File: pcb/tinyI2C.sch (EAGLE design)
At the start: 37 parts, among them IC1 74LVC1G125DCK, IC2 74LVC1G125DCK, IC3 IC_LDO_MIC5355, U1 LPC824M201JHI33, X1 TSW-112-02-S-S, X2 TSW-112-02-S-S, X3 TSW-106-02-S-S-RA, X4 TSW-102-02-S-S, X5 TSW-102-02-S-S, X6 TSW-102-02-S-S

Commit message: [ PCB ][ SCH ] R, C, BOM
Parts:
- C1, C2, C6, C7: value 1005 -> 0.1u/1005
- C3, C4, C5: value 1005 -> 10u/1005
- C8, C9: value 1005 -> 18p/1005
- Q1: value (none) -> 12MHz
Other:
- moved on the sheet: C2, C3, C4, C5, C6, IC3, TP1, TP2, TP3, TP6, TP7, X4-2

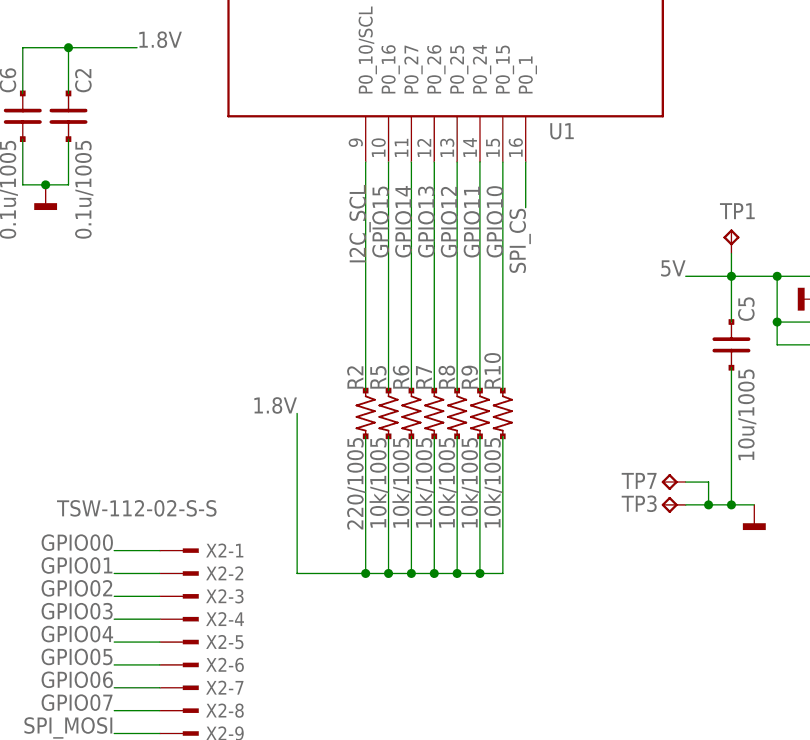
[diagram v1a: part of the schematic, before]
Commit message: [ PCB ] Q1 silk
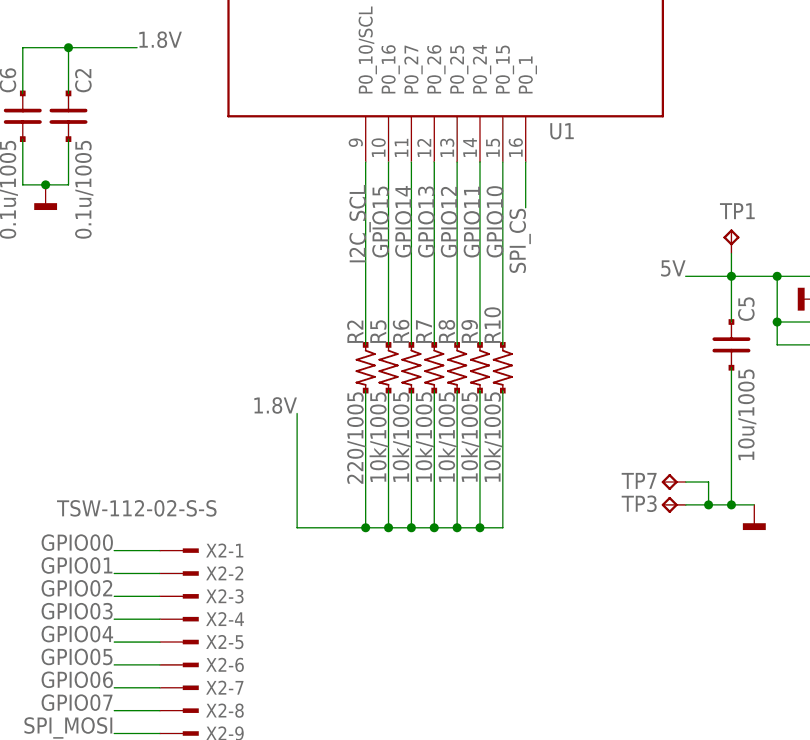
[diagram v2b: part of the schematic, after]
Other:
- moved on the sheet: R10, R2, R5, R6, R7, R8, R9
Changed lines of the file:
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@@
 </instance>
 <instance part="R1" gate="G$1" x="81.28" y="129.54" rot="R90"/>
-<instance part="R2" gate="G$1" x="127" y="55.88" rot="R270"/>
+<instance part="R2" gate="G$1" x="127" y="60.96" rot="R270"/>
 <instance part="R3" gate="G$1" x="86.36" y="129.54" rot="R90"/>
 <instance part="R4" gate="G$1" x="83.82" y="129.54" rot="R90"/>
-<instance part="R5" gate="G$1" x="129.54" y="55.88" rot="R270"/>
-<instance part="R6" gate="G$1" x="132.08" y="55.88" rot="R270"/>
-<instance part="R7" gate="G$1" x="134.62" y="55.88" rot="R270"/>
-<instance part="R8" gate="G$1" x="137.16" y="55.88" rot="R270"/>
-<instance part="R9" gate="G$1" x="139.7" y="55.88" rot="R270"/>
-<instance part="R10" gate="G$1" x="142.24" y="55.88" rot="R270"/>
+<instance part="R5" gate="G$1" x="129.54" y="60.96" rot="R270"/>
+<instance part="R6" gate="G$1" x="132.08" y="60.96" rot="R270"/>
+<instance part="R7" gate="G$1" x="134.62" y="60.96" rot="R270"/>
+<instance part="R8" gate="G$1" x="137.16" y="60.96" rot="R270"/>
+<instance part="R9" gate="G$1" x="139.7" y="60.96" rot="R270"/>
+<instance part="R10" gate="G$1" x="142.24" y="60.96" rot="R270"/>
 <instance part="C3" gate="G$1" x="231.14" y="63.5"/>
 <instance part="GND1" gate="1" x="231.14" y="48.26"/>
@@
 <segment>
 <pinref part="R2" gate="G$1" pin="2"/>
-<wire x1="127" y1="53.34" x2="127" y2="38.1" width="0.1524" layer="91"/>
+<wire x1="127" y1="58.42" x2="127" y2="43.18" width="0.1524" layer="91"/>
 <label x="119.38" y="55.88" size="1.778" layer="95" rot="MR0"/>
 <pinref part="R5" gate="G$1" pin="2"/>
-<wire x1="127" y1="38.1" x2="119.38" y2="38.1" width="0.1524" layer="91"/>
-<wire x1="119.38" y1="38.1" x2="119.38" y2="55.88" width="0.1524" layer="91"/>
-<wire x1="129.54" y1="53.34" x2="129.54" y2="38.1" width="0.1524" layer="91"/>
-<wire x1="129.54" y1="38.1" x2="127" y2="38.1" width="0.1524" layer="91"/>
-<junction x="127" y="38.1"/>
+<wire x1="127" y1="43.18" x2="119.38" y2="43.18" width="0.1524" layer="91"/>
+<wire x1="119.38" y1="43.18" x2="119.38" y2="55.88" width="0.1524" layer="91"/>
+<wire x1="129.54" y1="58.42" x2="129.54" y2="43.18" width="0.1524" layer="91"/>
+<wire x1="129.54" y1="43.18" x2="127" y2="43.18" width="0.1524" layer="91"/>
+<junction x="127" y="43.18"/>
 <pinref part="R6" gate="G$1" pin="2"/>
-<wire x1="132.08" y1="53.34" x2="132.08" y2="38.1" width="0.1524" layer="91"/>
-<wire x1="132.08" y1="38.1" x2="129.54" y2="38.1" width="0.1524" layer="91"/>
-<junction x="129.54" y="38.1"/>
+<wire x1="132.08" y1="58.42" x2="132.08" y2="43.18" width="0.1524" layer="91"/>
+<wire x1="132.08" y1="43.18" x2="129.54" y2="43.18" width="0.1524" layer="91"/>
+<junction x="129.54" y="43.18"/>
 <pinref part="R7" gate="G$1" pin="2"/>
-<wire x1="134.62" y1="53.34" x2="134.62" y2="38.1" width="0.1524" layer="91"/>
-<wire x1="134.62" y1="38.1" x2="132.08" y2="38.1" width="0.1524" layer="91"/>
-<junction x="132.08" y="38.1"/>
+<wire x1="134.62" y1="58.42" x2="134.62" y2="43.18" width="0.1524" layer="91"/>
+<wire x1="134.62" y1="43.18" x2="132.08" y2="43.18" width="0.1524" layer="91"/>
+<junction x="132.08" y="43.18"/>
 <pinref part="R8" gate="G$1" pin="2"/>
-<wire x1="137.16" y1="53.34" x2="137.16" y2="38.1" width="0.1524" layer="91"/>
-<wire x1="137.16" y1="38.1" x2="134.62" y2="38.1" width="0.1524" layer="91"/>
-<junction x="134.62" y="38.1"/>
+<wire x1="137.16" y1="58.42" x2="137.16" y2="43.18" width="0.1524" layer="91"/>
+<wire x1="137.16" y1="43.18" x2="134.62" y2="43.18" width="0.1524" layer="91"/>
+<junction x="134.62" y="43.18"/>
 <pinref part="R9" gate="G$1" pin="2"/>
-<wire x1="139.7" y1="53.34" x2="139.7" y2="38.1" width="0.1524" layer="91"/>
-<wire x1="139.7" y1="38.1" x2="137.16" y2="38.1" width="0.1524" layer="91"/>
-<junction x="137.16" y="38.1"/>
+<wire x1="139.7" y1="58.42" x2="139.7" y2="43.18" width="0.1524" layer="91"/>
+<wire x1="139.7" y1="43.18" x2="137.16" y2="43.18" width="0.1524" layer="91"/>
+<junction x="137.16" y="43.18"/>
 <pinref part="R10" gate="G$1" pin="2"/>
-<wire x1="142.24" y1="53.34" x2="142.24" y2="38.1" width="0.1524" layer="91"/>
-<wire x1="142.24" y1="38.1" x2="139.7" y2="38.1" width="0.1524" layer="91"/>
-<junction x="139.7" y="38.1"/>
+<wire x1="142.24" y1="58.42" x2="142.24" y2="43.18" width="0.1524" layer="91"/>
+<wire x1="142.24" y1="43.18" x2="139.7" y2="43.18" width="0.1524" layer="91"/>
+<junction x="139.7" y="43.18"/>
 </segment>
 <segment>
@@
 <pinref part="U1" gate="G$1" pin="P0_10/SCL"/>
 <label x="127" y="81.28" size="1.778" layer="95" rot="MR270"/>
-<wire x1="127" y1="83.82" x2="127" y2="58.42" width="0.1524" layer="91"/>
+<wire x1="127" y1="83.82" x2="127" y2="63.5" width="0.1524" layer="91"/>
 <pinref part="R2" gate="G$1" pin="1"/>
 </segment>
@@
 <pinref part="U1" gate="G$1" pin="P0_16"/>
 <label x="129.54" y="81.28" size="1.778" layer="95" rot="MR270"/>
-<wire x1="129.54" y1="83.82" x2="129.54" y2="58.42" width="0.1524" layer="91"/>
+<wire x1="129.54" y1="83.82" x2="129.54" y2="63.5" width="0.1524" layer="91"/>
 <pinref part="R5" gate="G$1" pin="1"/>
 </segment>
@@
 <label x="132.08" y="81.28" size="1.778" layer="95" rot="MR270"/>
 <pinref part="R6" gate="G$1" pin="1"/>
-<wire x1="132.08" y1="58.42" x2="132.08" y2="83.82" width="0.1524" layer="91"/>
+<wire x1="132.08" y1="63.5" x2="132.08" y2="83.82" width="0.1524" layer="91"/>
 </segment>
 <segment>
@@
 <label x="134.62" y="81.28" size="1.778" layer="95" rot="MR270"/>
 <pinref part="R7" gate="G$1" pin="1"/>
-<wire x1="134.62" y1="58.42" x2="134.62" y2="83.82" width="0.1524" layer="91"/>
+<wire x1="134.62" y1="63.5" x2="134.62" y2="83.82" width="0.1524" layer="91"/>
 </segment>
 <segment>
@@
 <label x="137.16" y="81.28" size="1.778" layer="95" rot="MR270"/>
 <pinref part="R8" gate="G$1" pin="1"/>
-<wire x1="137.16" y1="58.42" x2="137.16" y2="83.82" width="0.1524" layer="91"/>
+<wire x1="137.16" y1="63.5" x2="137.16" y2="83.82" width="0.1524" layer="91"/>
 </segment>
 <segment>
@@
 <label x="139.7" y="81.28" size="1.778" layer="95" rot="MR270"/>
 <pinref part="R9" gate="G$1" pin="1"/>
-<wire x1="139.7" y1="58.42" x2="139.7" y2="83.82" width="0.1524" layer="91"/>
+<wire x1="139.7" y1="63.5" x2="139.7" y2="83.82" width="0.1524" layer="91"/>
 </segment>
 <segment>
@@
 <label x="142.24" y="81.28" size="1.778" layer="95" rot="MR270"/>
 <pinref part="R10" gate="G$1" pin="1"/>
-<wire x1="142.24" y1="58.42" x2="142.24" y2="83.82" width="0.1524" layer="91"/>
-</segment>
-<segment>
+<wire x1="142.24" y1="63.5" x2="142.24" y2="83.82" width="0.1524" layer="91"/>
+</segment>
+<segment>

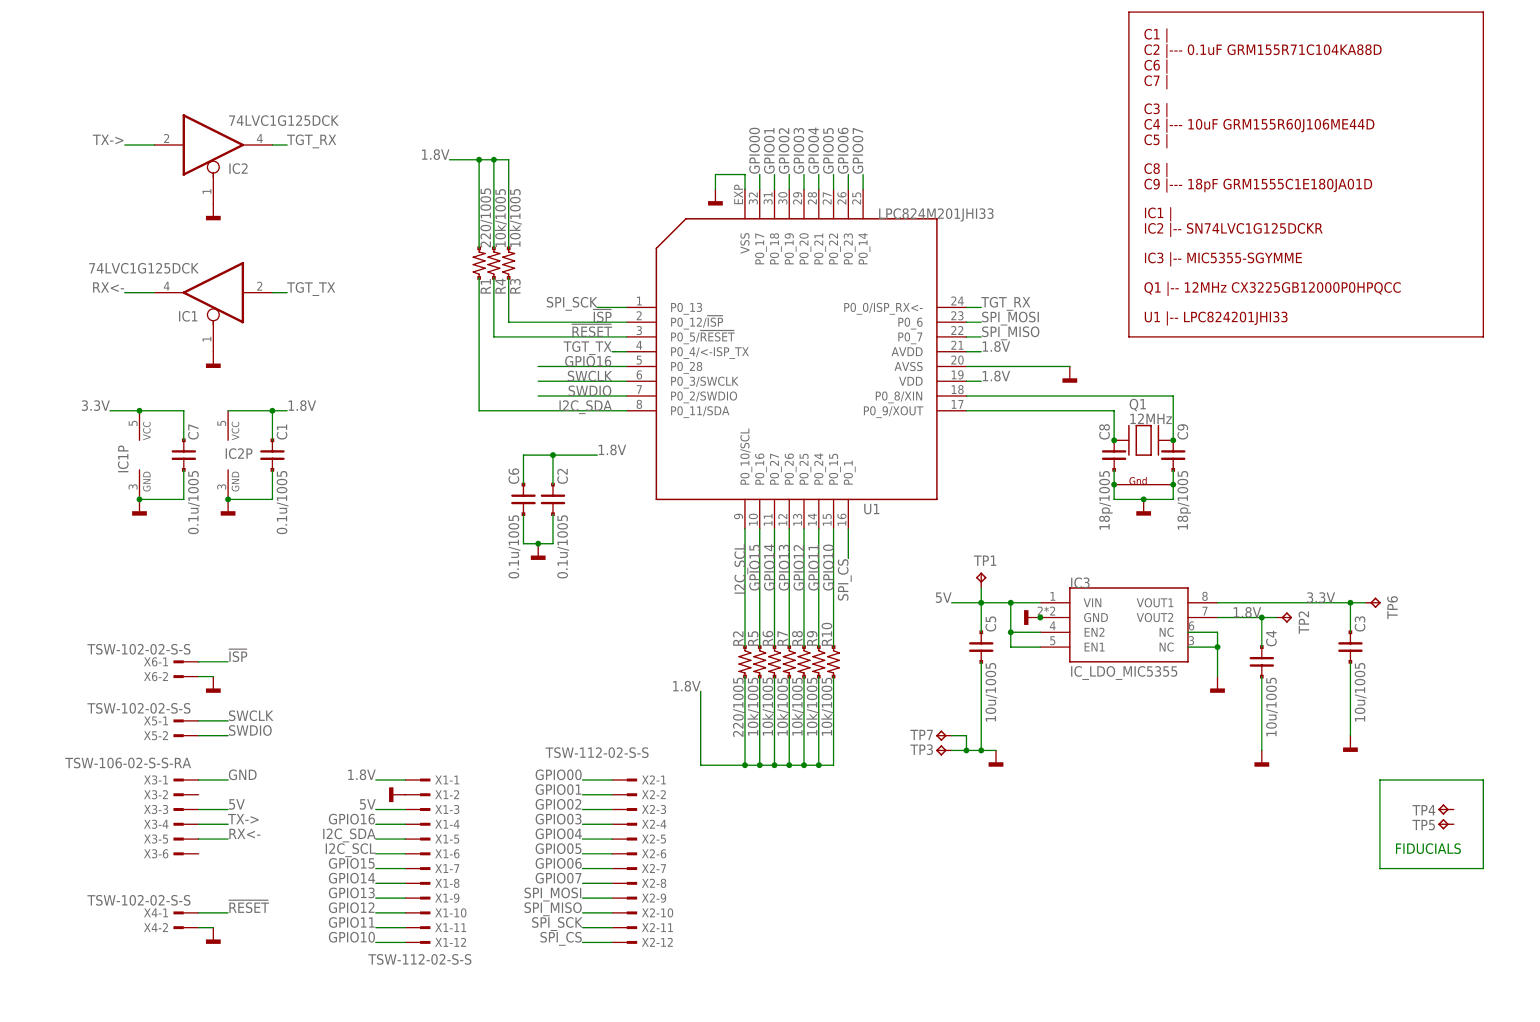
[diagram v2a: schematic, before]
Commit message: [ PCB ] add minlab icon;panel fix
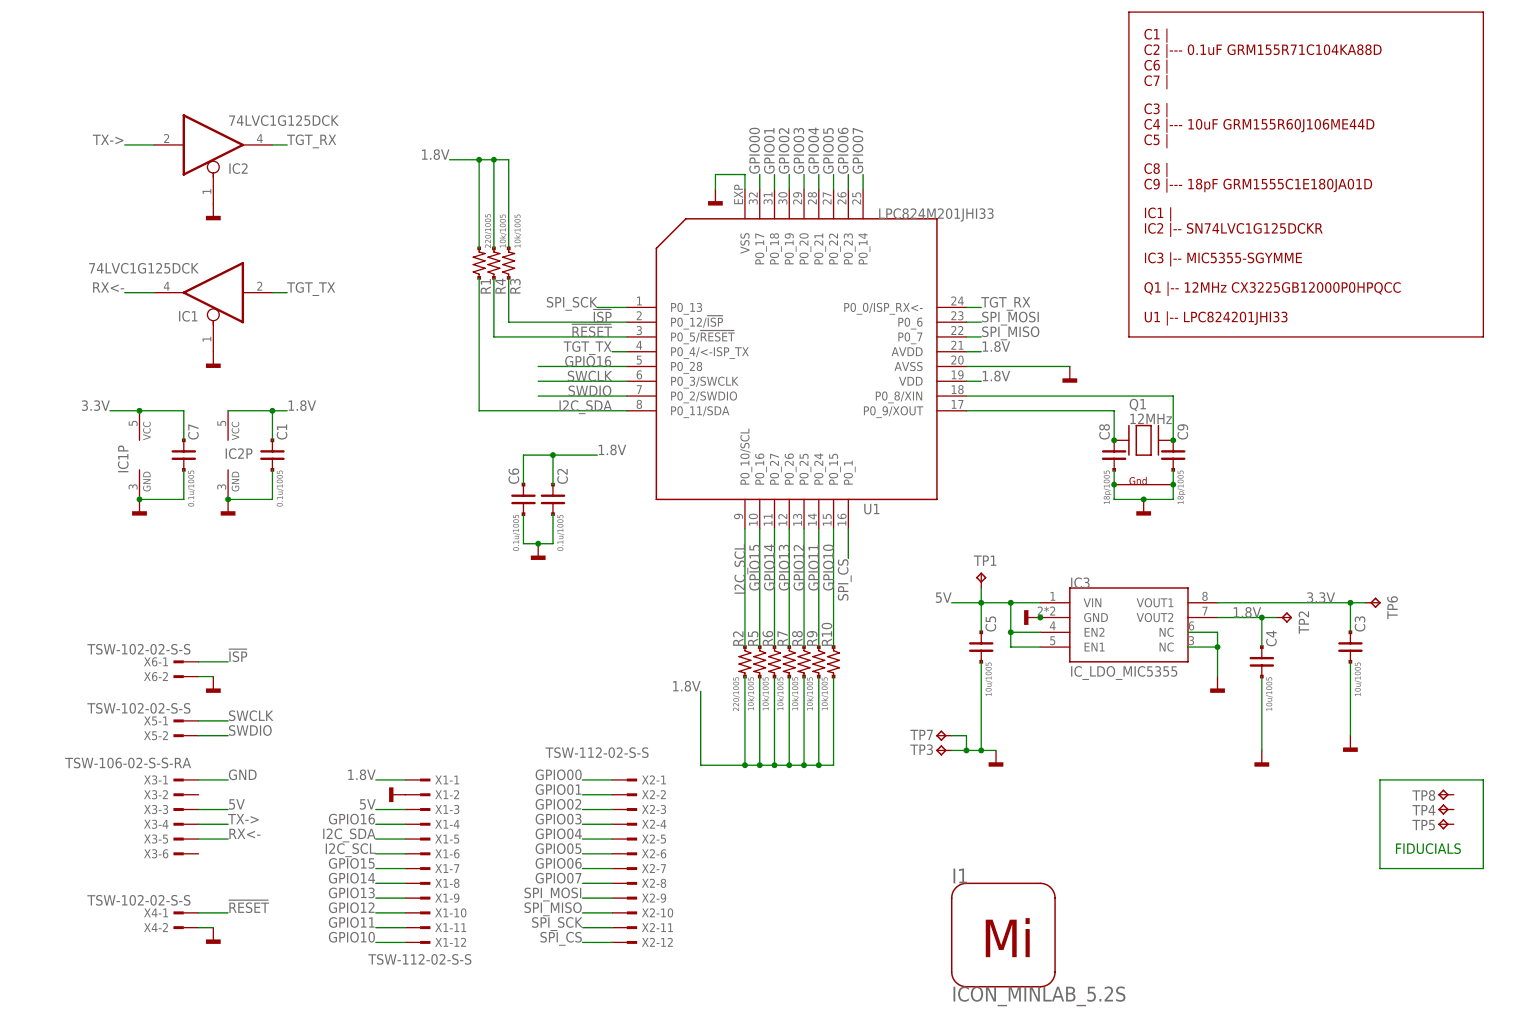
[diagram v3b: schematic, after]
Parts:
- added I1: ICON_MINLAB_5.2S, mylib:ICON_MINLAB_5.2S
- added TP8: TPTP10R, testpad:TPTP10R
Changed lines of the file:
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@@
 <layer number="132" name="bAdjust" color="7" fill="1" visible="no" active="yes"/>
 <layer number="144" name="Drill_legend" color="7" fill="1" visible="no" active="yes"/>
+<layer number="145" name="DrillLegend_01-16" color="2" fill="9" visible="no" active="yes"/>
+<layer number="146" name="DrillLegend_01-20" color="3" fill="9" visible="no" active="yes"/>
 <layer number="151" name="HeatSink" color="7" fill="1" visible="no" active="yes"/>
 <layer number="152" name="_bDocu" color="7" fill="1" visible="no" active="yes"/>
@@
 <part name="GND16" library="mbed-HDK" deviceset="GND" device=""/>
 <part name="TP7" library="testpad_local" deviceset="TP" device="B1,27" value="TPB1,27"/>
+<part name="TP8" library="testpad" deviceset="TP" device="TP10R" value="TPTP10R"/>
+<part name="I1" library="mylib" deviceset="ICON_MINLAB" device="_5.2S" value="ICON_MINLAB_5.2S"/>
 </parts>
 <sheets>
@@
 <attribute name="TP_SIGNAL_NAME" x="161.29" y="49.53" size="1.778" layer="97" rot="R90"/>
 </instance>
+<instance part="TP8" gate="G$1" x="246.38" y="38.1" smashed="yes" rot="R90">
+<attribute name="NAME" x="245.872" y="37.084" size="1.778" layer="95" rot="MR0"/>
+<attribute name="TP_SIGNAL_NAME" x="247.65" y="39.37" size="1.778" layer="97" rot="R90"/>
+</instance>
+<instance part="I1" gate="G$1" x="162.56" y="5.08"/>
 </instances>
 <busses>

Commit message: [ PCB ] library update
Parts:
- TP4, TP5, TP8: value TPTP10R -> TPTP20R; device testpad:TPTP10R -> testpad_local:TPTP20R
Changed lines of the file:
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@@
 <layers>
 <layer number="1" name="Top" color="4" fill="1" visible="no" active="no"/>
+<layer number="2" name="Route2" color="1" fill="3" visible="no" active="no"/>
+<layer number="3" name="Route3" color="4" fill="3" visible="no" active="no"/>
+<layer number="14" name="Route14" color="1" fill="6" visible="no" active="no"/>
+<layer number="15" name="Route15" color="4" fill="6" visible="no" active="no"/>
 <layer number="16" name="Bottom" color="1" fill="1" visible="no" active="no"/>
 <layer number="17" name="Pads" color="2" fill="1" visible="no" active="no"/>
@@
 <part name="X4" library="con-samtec.local" deviceset="TSW-102-02-S-S" device=""/>
 <part name="GND12" library="mbed-HDK" deviceset="GND" device=""/>
-<part name="TP4" library="testpad" deviceset="TP" device="TP10R" value="TPTP10R"/>
-<part name="TP5" library="testpad" deviceset="TP" device="TP10R" value="TPTP10R"/>
+<part name="TP4" library="testpad_local" deviceset="TP" device="TP20R" value="TPTP20R"/>
+<part name="TP5" library="testpad_local" deviceset="TP" device="TP20R" value="TPTP20R"/>
 <part name="X5" library="con-samtec.local" deviceset="TSW-102-02-S-S" device=""/>
 <part name="X6" library="con-samtec.local" deviceset="TSW-102-02-S-S" device=""/>
@@
 <part name="GND16" library="mbed-HDK" deviceset="GND" device=""/>
 <part name="TP7" library="testpad_local" deviceset="TP" device="B1,27" value="TPB1,27"/>
-<part name="TP8" library="testpad" deviceset="TP" device="TP10R" value="TPTP10R"/>
+<part name="TP8" library="testpad_local" deviceset="TP" device="TP20R" value="TPTP20R"/>
 <part name="I1" library="mylib" deviceset="ICON_MINLAB" device="_5.2S" value="ICON_MINLAB_5.2S"/>
 </parts>

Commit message: .
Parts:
- removed TP6: TPTP07R, testpad_local:TPTP07R
- TP2: value TPTP07R -> TESTPAD; device testpad_local:TPTP07R -> mylib:TESTPAD
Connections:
- net 1.8V: now also TP2.1; no longer TP2.TP
- net 3.3V: no longer TP6.TP
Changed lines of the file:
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@@
 <part name="GND11" library="mbed-HDK" deviceset="GND" device=""/>
 <part name="TP1" library="testpad_local" deviceset="TP" device="TP07R"/>
-<part name="TP2" library="testpad_local" deviceset="TP" device="TP07R"/>
 <part name="TP3" library="testpad_local" deviceset="TP" device="B1,27" value="TPB1,27"/>
 <part name="R1" library="mylib" deviceset="R_US_PAD_PAD" device="_1005" value="220/1005"/>
@@
 <part name="GND14" library="mbed-HDK" deviceset="GND" device=""/>
 <part name="GND15" library="mbed-HDK" deviceset="GND" device=""/>
-<part name="TP6" library="testpad_local" deviceset="TP" device="TP07R"/>
 <part name="IC1" library="74xx-little-us_local" deviceset="74*1G125" device="DCK" technology="LVC"/>
 <part name="IC2" library="74xx-little-us_local" deviceset="74*1G125" device="DCK" technology="LVC"/>
@@
 <part name="TP8" library="testpad_local" deviceset="TP" device="TP20R" value="TPTP20R"/>
 <part name="I1" library="mylib" deviceset="ICON_MINLAB" device="_5.2S" value="ICON_MINLAB_5.2S"/>
+<part name="TP2" library="mylib" deviceset="TESTPAD" device=""/>
 </parts>
 <sheets>
@@
 <attribute name="TP_SIGNAL_NAME" x="168.91" y="74.93" size="1.778" layer="97"/>
 </instance>
-<instance part="TP2" gate="G$1" x="220.98" y="68.58" smashed="yes" rot="R270">
-<attribute name="NAME" x="222.25" y="69.85" size="1.778" layer="95" rot="R270"/>
-<attribute name="TP_SIGNAL_NAME" x="219.71" y="67.31" size="1.778" layer="97" rot="R270"/>
-</instance>
 <instance part="TP3" gate="G$1" x="160.02" y="45.72" smashed="yes" rot="R90">
 <attribute name="NAME" x="159.512" y="46.736" size="1.778" layer="95" rot="R180"/>
@@
 <instance part="GND14" gate="1" x="35.56" y="58.42"/>
 <instance part="GND15" gate="1" x="177.8" y="68.58" rot="R270"/>
-<instance part="TP6" gate="G$1" x="236.22" y="71.12" smashed="yes" rot="R270">
-<attribute name="NAME" x="237.49" y="72.39" size="1.778" layer="95" rot="R270"/>
-<attribute name="TP_SIGNAL_NAME" x="234.95" y="69.85" size="1.778" layer="97" rot="R270"/>
-</instance>
 <instance part="IC1" gate="A" x="35.56" y="124.46" smashed="yes" rot="R180">
 <attribute name="NAME" x="33.02" y="121.285" size="1.778" layer="95" rot="R180"/>
@@
 </instance>
 <instance part="I1" gate="G$1" x="162.56" y="5.08"/>
+<instance part="TP2" gate="1" x="220.98" y="68.58"/>
 </instances>
 <busses>
@@
 <wire x1="215.9" y1="63.5" x2="215.9" y2="68.58" width="0.1524" layer="91"/>
 <junction x="215.9" y="68.58"/>
-<pinref part="TP2" gate="G$1" pin="TP"/>
 <wire x1="208.28" y1="68.58" x2="215.9" y2="68.58" width="0.1524" layer="91"/>
+<pinref part="TP2" gate="1" pin="1"/>
 </segment>
 </net>
@@
 <pinref part="IC3" gate="G$1" pin="VOUT1"/>
 <pinref part="C3" gate="G$1" pin="1"/>
-<pinref part="TP6" gate="G$1" pin="TP"/>
 <wire x1="208.28" y1="71.12" x2="231.14" y2="71.12" width="0.1524" layer="91"/>
-<wire x1="231.14" y1="71.12" x2="233.68" y2="71.12" width="0.1524" layer="91"/>
 <wire x1="231.14" y1="66.04" x2="231.14" y2="71.12" width="0.1524" layer="91"/>
-<junction x="231.14" y="71.12"/>
-</segment>
-<segment>
+</segment>
+<segment>
